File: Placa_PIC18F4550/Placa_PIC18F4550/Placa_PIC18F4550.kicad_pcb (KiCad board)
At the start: 2 copper layers, 71.1 x 95.2 mm, 33 parts, among them J1 PORTD, J10 USB_B, J11 PICKIT, J2 PORTA, J3 PORTE, J4 PORTB, J5 PORTC, J6 GND, J7 Vol, J8 Volt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

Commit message: Modificación de archivos Gerber!
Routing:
- net /RD7: track 0.00 -> 20.3 mm
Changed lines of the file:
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@@
     (thickness 1.6)
     (drawings 33)
-    (tracks 219)
+    (tracks 220)
     (zones 0)
     (modules 33)
@@
     (32 B.Adhes user)
     (33 F.Adhes user)
-    (34 B.Paste user)
+    (34 B.Paste user hide)
     (35 F.Paste user)
     (36 B.SilkS user)
-    (37 F.SilkS user)
+    (37 F.SilkS user hide)
     (38 B.Mask user)
     (39 F.Mask user)
@@
   (segment (start 97.79 123.19) (end 118.11 123.19) (width 0.254) (layer B.Cu) (net 15))
   (segment (start 97.79 120.65) (end 118.11 120.65) (width 0.254) (layer B.Cu) (net 16))
+  (segment (start 97.79 118.11) (end 118.11 118.11) (width 0.25) (layer B.Cu) (net 17))
   (segment (start 82.55 107.95) (end 58.42 107.95) (width 0.254) (layer B.Cu) (net 18))
   (segment (start 82.55 105.41) (end 58.42 105.41) (width 0.254) (layer B.Cu) (net 19))

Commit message: Actualicación de documentos
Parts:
- moved C1 1.90 mm to (76.8, 135.9), turned to 180 degrees
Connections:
- C1 pad 1: GND -> Net-(C1-Pad1)
- C1 pad 2: Net-(C1-Pad2) -> GND
- U1 pad 18: Net-(C1-Pad2) -> Net-(C1-Pad1)
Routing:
- net /RD7: track 20.3 -> 0.00 mm
- net Net-(C1-Pad1): track 0.00 -> 5.72 mm
- net Net-(C1-Pad2): track 5.12 -> 0.00 mm
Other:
- board text added: "#ProgramandoCon39Pines"

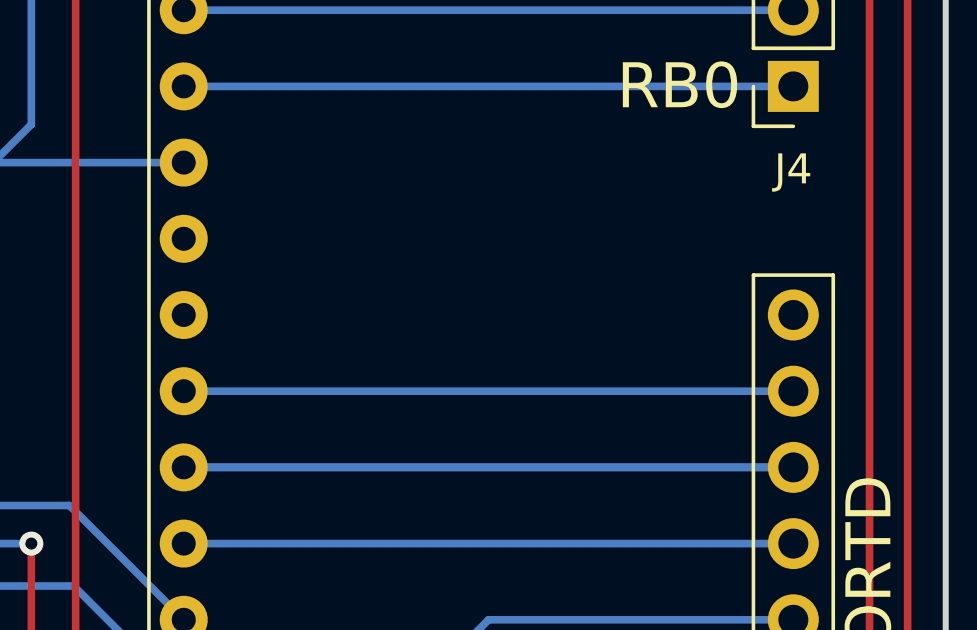
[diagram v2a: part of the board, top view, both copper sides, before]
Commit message: EEPROM Variables
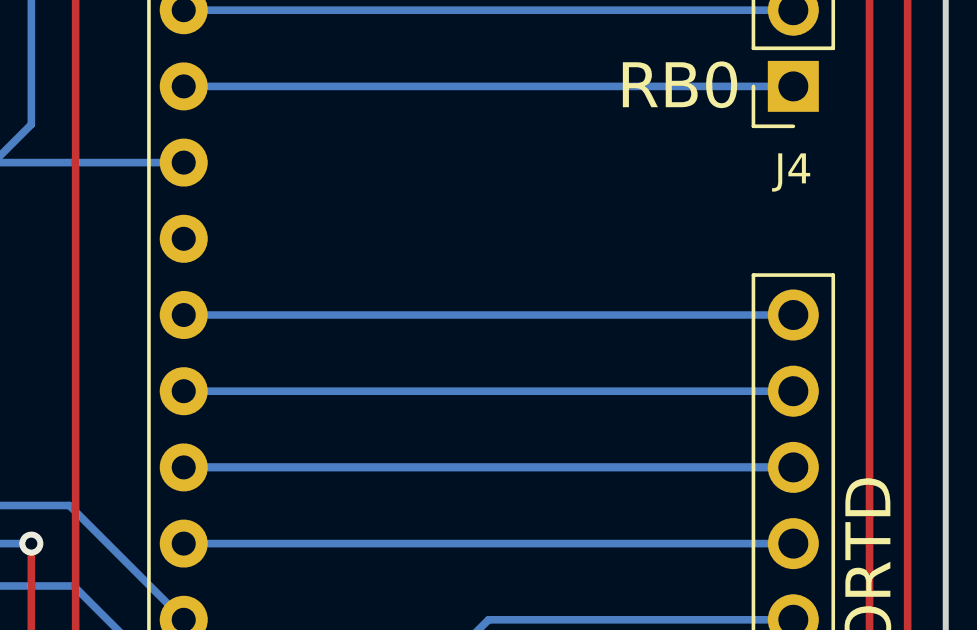
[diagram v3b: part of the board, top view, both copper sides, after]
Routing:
- net /RD7: track 0.00 -> 20.3 mm
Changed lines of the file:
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@@
     (thickness 1.6)
     (drawings 34)
-    (tracks 219)
+    (tracks 220)
     (zones 0)
     (modules 33)
@@
   )
   (setup
-    (last_trace_width 0.254)
+    (last_trace_width 0.25)
     (user_trace_width 0.127)
     (user_trace_width 0.254)
@@
   (segment (start 97.79 123.19) (end 118.11 123.19) (width 0.254) (layer B.Cu) (net 14))
   (segment (start 97.79 120.65) (end 118.11 120.65) (width 0.254) (layer B.Cu) (net 15))
+  (segment (start 118.11 118.11) (end 97.79 118.11) (width 0.25) (layer B.Cu) (net 16))
   (segment (start 82.55 107.95) (end 58.42 107.95) (width 0.254) (layer B.Cu) (net 17))
   (segment (start 82.55 105.41) (end 58.42 105.41) (width 0.254) (layer B.Cu) (net 18))

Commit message: Programa SPI
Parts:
- added J12: Conn_01x02_Male, Connector_PinHeader_2.54mm:PinHeader_1x02_P2.54mm_Vertical, F.Cu at (114.3, 138.4)
- Q1: footprint Package_TO_SOT_THT:TO-92_Inline -> Package_TO_SOT_THT:TO-92L_Inline_Wide
- moved G*** 4.02 mm to (108.0, 99.1)
- moved Q1 2.54 mm to (77.5, 73.7)
- moved D1 1.27 mm to (104.1, 142.2)
- moved R2 1.27 mm to (118.1, 142.2)
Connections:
- R2 pad 1: /RD0 -> Net-(J12-Pad1)
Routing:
- net Net-(J12-Pad1): track 0.00 -> 6.88 mm
- net /RC5: track 130.9 -> 132.3 mm
- net /Vc: track 146.3 -> 145.7 mm
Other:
- board text added: "PLACA PIC18F4550 V 1.01"
- board text removed: "PLACA PIC18F4550 V 1.0"
